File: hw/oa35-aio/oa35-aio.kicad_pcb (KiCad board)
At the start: 6 copper layers, 36 x 36 mm, 283 parts, among them J1 TYPE-C-31-M-12, J10 M1A, J11 M1B, J12 M1C, J13 M2A, J14 M2B, J15 M2C, J16 M3A, J17 M3B, J18 M3C, J19 M4A, J2 SM06B-SRSS-TB, J20 M4B, J21 M4C, J3 BAT+, J4 BAT-, P1 +5V, P10 TX6, P11 RX1, P12 TX1, P13 LED, P14 BZ-, P15 BZ+, P16 RSSI, P17 SCL, P18 SDA, P19 +3V3, P2 GND, P20 GND, P21 VBAT, P22 GND, P3 RX2, P4 TX2, P5 +5V, P6 GND, P7 RX4, P8 TX4, P9 RX6, Q1 2N7002, U1 INA186A3IDCKR, U10 USBLC6-2SC6, U2 LMR51430YFDDCR, U20 AT32F421G8U7, U21 NSG2065Q, U3 LMR51430YFDDCR, U30 AT32F421G8U7, U31 NSG2065Q, U4 LP5912-3.3DRVR, U40 AT32F421G8U7, U41 NSG2065Q, U5 TLV76733DRVR, U50 AT32F421G8U7, U51 NSG2065Q, U6 STM32F722RET6, U7 ICM-42688-P, U8 BMP280, U9 W25Q128JVSIQ, Y1 8MHz

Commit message: OA35-AIO: routing round 2, 103 of 200 signal nets in copper
Co-Authored-By: Claude Opus 5 <noreply@anthropic.com>
Claude-Session: https://claude.ai/code/session_013J1rgXZWykCJN7jVVS67P2
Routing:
- net FBB_2: track 0.00 -> 46.5 mm, vias 0 -> 3
- net PH_A_2: track 9.21 -> 51.7 mm, vias 0 -> 3
- net FBC_2: track 0.00 -> 40.7 mm, vias 0 -> 2
- net CURR: track 0.00 -> 39.9 mm, vias 0 -> 3
- net M4: track 0.00 -> 29.9 mm, vias 0 -> 2
- net PH_C_2: track 21.1 -> 47.7 mm, vias 2 -> 4
- net PH_B_3: track 1.30 -> 24.0 mm, vias 0 -> 1
- net +10V: track 13.9 -> 32.6 mm, vias 1 -> 2
- net FBA_3: track 0.00 -> 18.6 mm, vias 0 -> 2
- net +5V: track 38.0 -> 55.7 mm, vias 0 -> 2
- net GLA_2: track 0.00 -> 17.0 mm, vias 0 -> 2
- net VBAT_IN: track 36.2 -> 53.0 mm, vias 0 -> 2
- net M2: track 0.00 -> 16.3 mm, vias 0 -> 2
- net BOOTA_4: track 0.00 -> 16.0 mm, vias 0 -> 2
- net +3V3: track 48.7 -> 64.4 mm, vias 1 -> 4
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
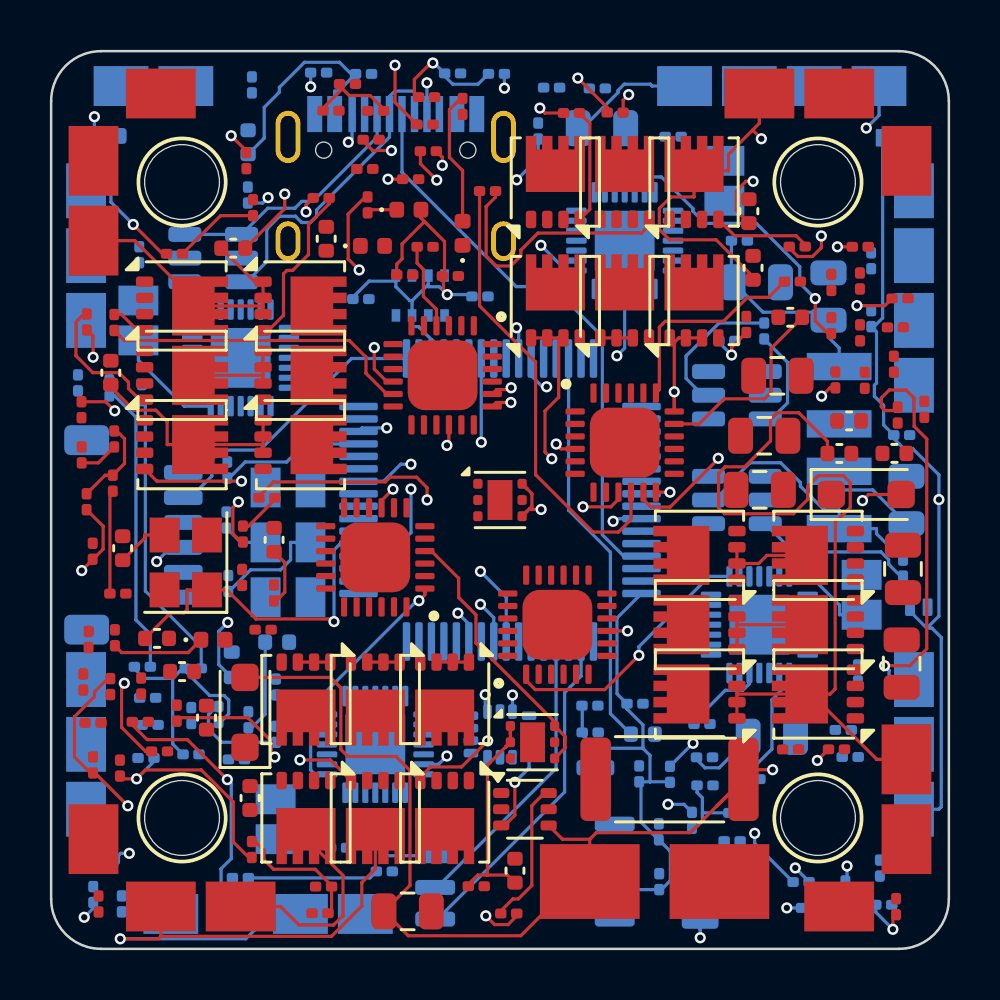
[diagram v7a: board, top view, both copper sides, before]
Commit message: OA35-AIO: snap the router's own output to the micron before feeding it back
freerouting works in tenths of a micron and returns wires whose ends miss
each other by a fraction of one.  That is invisible on a board, but handed
its own output back it warns 'the normalization of net failed' and then
never starts routing -- one round sat twelve minutes on the DSN load.  There
were 33 sub-micron segments; a micron is three orders of magnitude below
what a fabricator resolves, so rounding to it costs nothing.

A round that hangs anyway now hits a fifteen minute watchdog and stops the
series with the last routed board intact, instead of taking the run with it.

Co-Authored-By: Claude Opus 5 <noreply@anthropic.com>
Claude-Session: https://claude.ai/code/session_013J1rgXZWykCJN7jVVS67P2
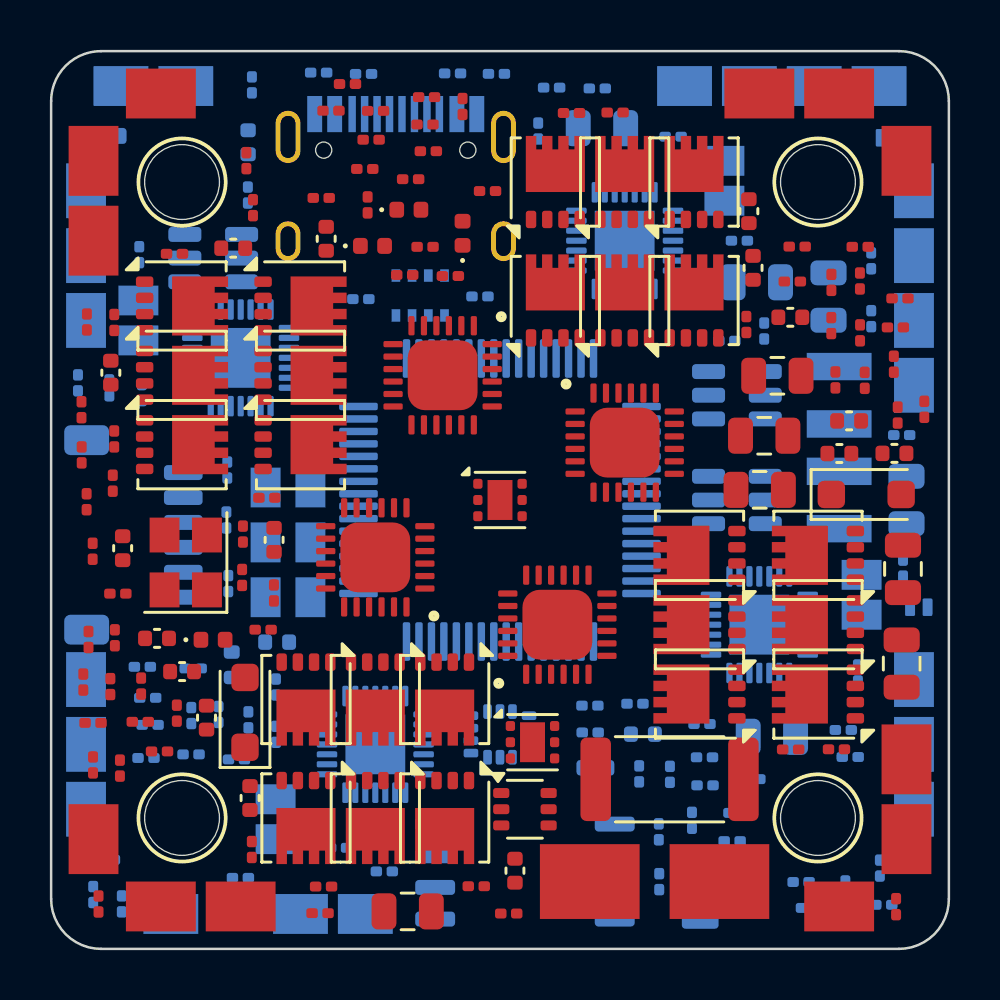
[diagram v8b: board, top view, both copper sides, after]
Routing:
- net +3V3: track 64.4 -> 0.00 mm, vias 4 -> 0
- net +5V: track 55.7 -> 0.00 mm, vias 2 -> 0
- net VBAT_IN: track 53.0 -> 0.00 mm, vias 2 -> 0
- net PH_A_2: track 51.7 -> 0.00 mm, vias 3 -> 0
- net PH_C_2: track 47.7 -> 0.00 mm, vias 4 -> 0
- net FBB_2: track 46.5 -> 0.00 mm, vias 3 -> 0
- net FBC_2: track 40.7 -> 0.00 mm, vias 2 -> 0
- net FBA_2: track 40.2 -> 0.00 mm, vias 3 -> 0
- net CURR: track 39.9 -> 0.00 mm, vias 3 -> 0
- net BEEP_G: track 33.5 -> 0.00 mm, vias 2 -> 0
- net PH_A_1: track 33.4 -> 0.00 mm
- net USB_DP: track 33.2 -> 0.00 mm
- net +10V: track 32.6 -> 0.00 mm, vias 2 -> 0
- net VDDA_2: track 30.6 -> 0.00 mm, vias 2 -> 0
- net M4: track 29.9 -> 0.00 mm, vias 2 -> 0
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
